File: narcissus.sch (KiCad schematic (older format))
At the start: 71 parts, among them J1 NEIGHBOR1, J2 NEIGHBOR2, U1 PCA9698, U2 PCA9698, U3 AP2553W6-7, U4 74HC4051

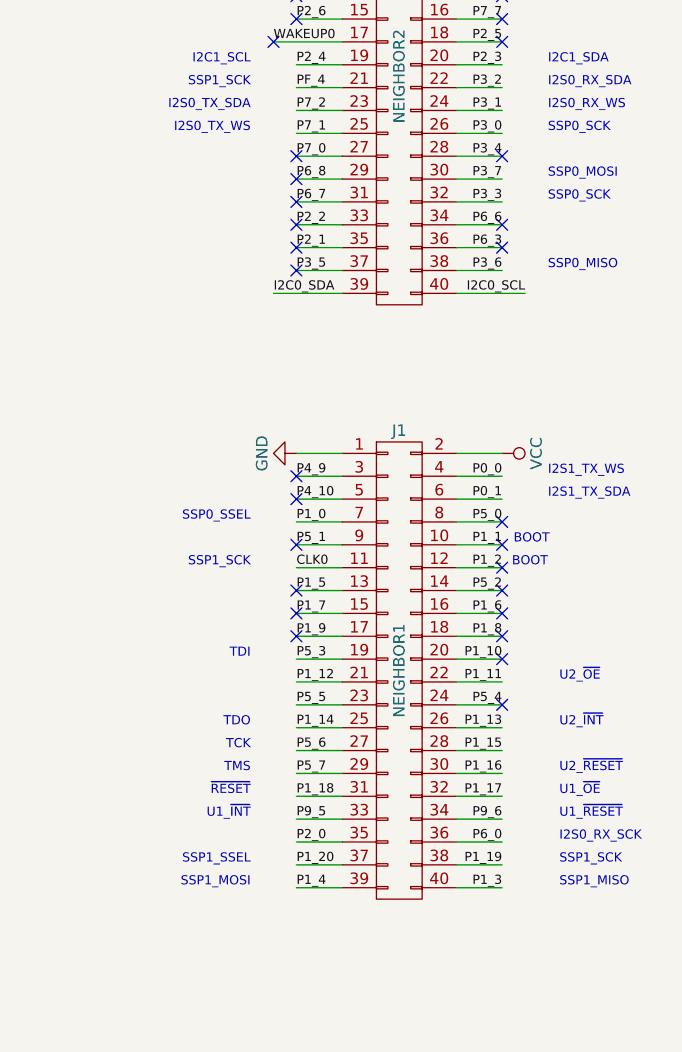
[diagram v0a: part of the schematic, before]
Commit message: adopt OSHWA convention for SPI signal names https://www.oshwa.org/a-resolution-to-redefine-spi-signal-names
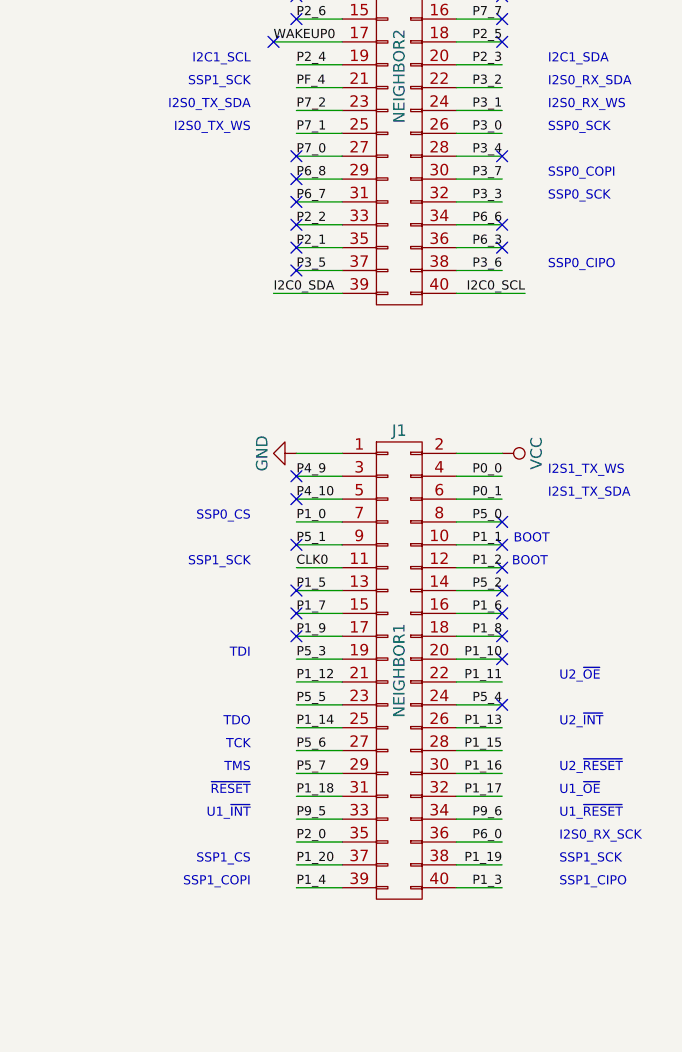
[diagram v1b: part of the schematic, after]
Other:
- note added: "SSP0_CIPO"
- note added: "SSP0_COPI"
- note added: "SSP0_CS"
- note added: "SSP1_CIPO"
- note added: "SSP1_COPI"
- note added: "SSP1_CS"
- note removed: "SSP0_MISO"
- note removed: "SSP0_MOSI"
- note removed: "SSP0_SSEL"
- note removed: "SSP1_MISO"
- note removed: "SSP1_MOSI"
- note removed: "SSP1_SSEL"
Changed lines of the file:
@@
 SSP0_SCK
 Text Notes 14350 5400 2    40   ~ 0
-SSP0_SSEL
+SSP0_CS
 Text Label 5450 1150 0    40   ~ 0
 P1_0
 Text Notes 15650 3900 0    40   ~ 0
-SSP0_MOSI
+SSP0_COPI
 Text Label 9300 2600 2    40   ~ 0
 P3_7
 Text Notes 15650 4300 0    40   ~ 0
-SSP0_MISO
+SSP0_CIPO
 Text Label 9300 2200 2    40   ~ 0
 P3_6
@@
 SSP1_SCK
 Text Notes 15700 7000 0    40   ~ 0
-SSP1_MISO
+SSP1_CIPO
 Text Notes 14350 6900 2    40   ~ 0
-SSP1_SSEL
+SSP1_CS
 Text Notes 14350 7000 2    40   ~ 0
-SSP1_MOSI
+SSP1_COPI
 Text Label 15450 6300 2    40   ~ 0
 P1_13
